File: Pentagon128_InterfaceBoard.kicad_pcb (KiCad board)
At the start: 2 copper layers, 150 x 119 mm, 42 parts, among them J1 DIN41612_02x32_AB, J10 Tape Out, J11 Tape In, J12 Mini-DIN-6, J14 Barrel_Jack_Switch, J2 Conn_02x03_Odd_Even ATmega Pr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, J3 Conn_02x08_Odd_Even Ext Keyb, J4 Conn_02x05_Odd_Even Kempston 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, J5 DE9_Plug Kempston Out SMD, J6 DE15_Plug_HighDensity VGA CRT, J7 Conn_01x04 FDD Power, J8 Conn_01x04 Audio In, J9 AudioJack3, Q1 Q_NPN_BCE, Q2 Q_NPN_BCE, Q3 Q_NPN_BCE, Q4 Q_NPN_BCE, U1 MT8816 PLCC44, U2 ATmega168PA-A

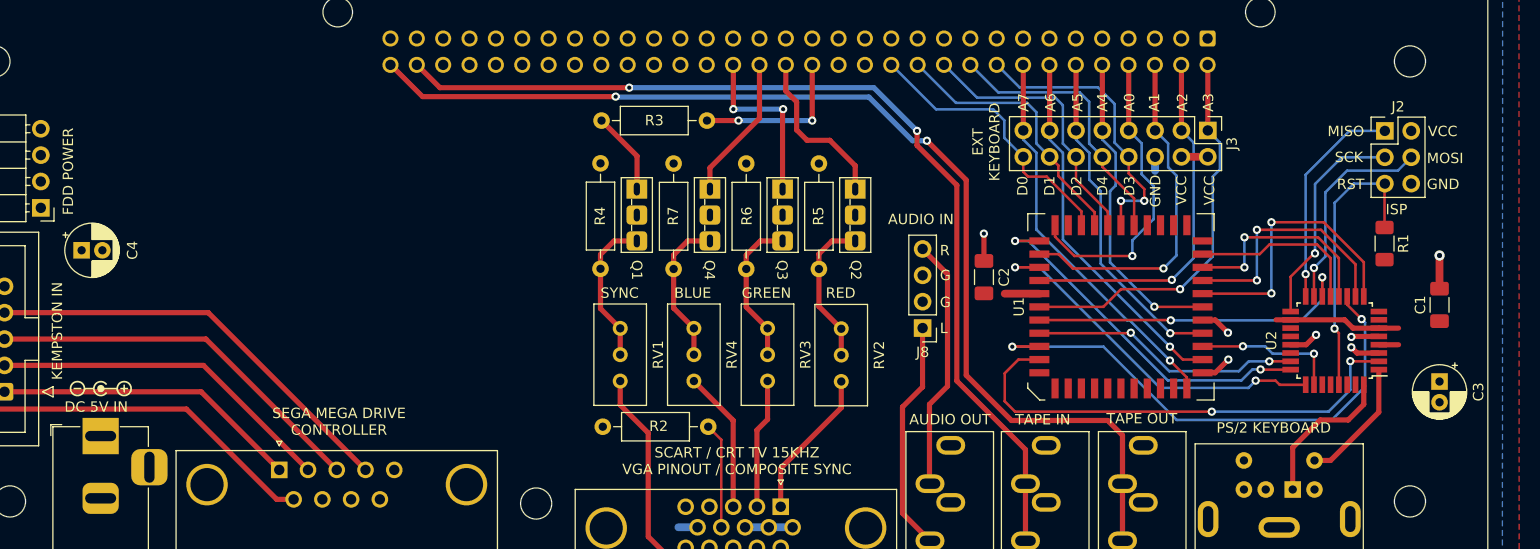
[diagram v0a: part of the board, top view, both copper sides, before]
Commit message: Intermediate variant based on review feedback. Added SN74LS07 oped drain buffers for switch matrix data lines output (questionable). Changes based on "AVR Microcontroller Hardware Design Considerations": - Blocking capacitor for ATmega moved close to power input pins, removed side VCC / GND connections. Not implemented: separate blocking caps for AVCC and all power pins pairs. - Added optional capacitor on ATmega RESET line connected to GND. Removed useless blocking capacitor for MT8816. Removed (possibly) useless electrolytic capacitors from PCB near ATmega and FDC Power connector.
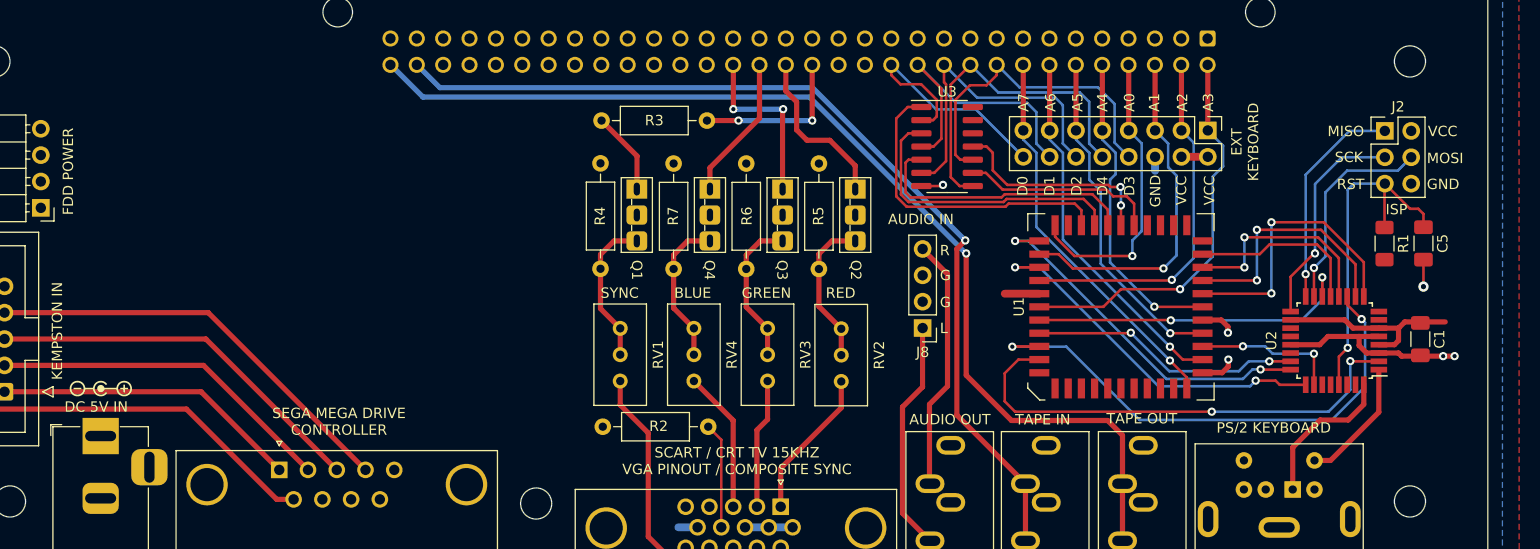
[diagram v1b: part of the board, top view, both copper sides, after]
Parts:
- removed C2: 0.1u, Capacitor_SMD:C_1206_3216Metric_Pad1.33x1.80mm_HandSolder
- removed C3, C4: 10u, Capacitor_THT:CP_Radial_D5.0mm_P2.00mm
- added C5: 0.1u, Capacitor_SMD:C_1206_3216Metric_Pad1.33x1.80mm_HandSolder, F.Cu at (198.4, 83.3)
- added U3: SN74LS07, Package_SO:SOIC-14_3.9x8.7mm_P1.27mm, F.Cu at (152.5, 74.0)
- moved C1 3.78 mm to (198.1, 92.6), turned to -90 degrees
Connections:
- U1 pad 33: /X4 -> Net-(U1-X4)
- U1 pad 34: /X3 -> Net-(U1-X3)
- U1 pad 35: /X2 -> Net-(U1-X2)
- U1 pad 36: /X1 -> Net-(U1-X1)
- U1 pad 37: /X0 -> Net-(U1-X0)
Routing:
- net Net-(U1-X0): track 0.00 -> 30.5 mm
- net Net-(U1-X1): track 0.00 -> 28.4 mm
- net Net-(U1-X2): track 0.00 -> 26.4 mm
- net Net-(U1-X3): track 0.00 -> 20.5 mm, vias 0 -> 2
- net Net-(U1-X4): track 0.00 -> 18.9 mm
- net GND: track 28.0 -> 38.6 mm, vias 7 -> 6
- net /X4: track 26.6 -> 32.8 mm
- net /RST: track 27.5 -> 33.4 mm
- net VCC: track 19.9 -> 24.6 mm
- net /X2: track 26.4 -> 30.7 mm
- net /TAPE_OUT: track 106.5 -> 102.3 mm, vias 2 -> 1
- net /X3: track 28.0 -> 31.7 mm, vias 2 -> 0
- net /TAPE_IN: track 94.6 -> 91.8 mm, vias 2 -> 1
- net /X1: track 26.5 -> 28.4 mm
- net /X0: track 27.3 -> 25.9 mm
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
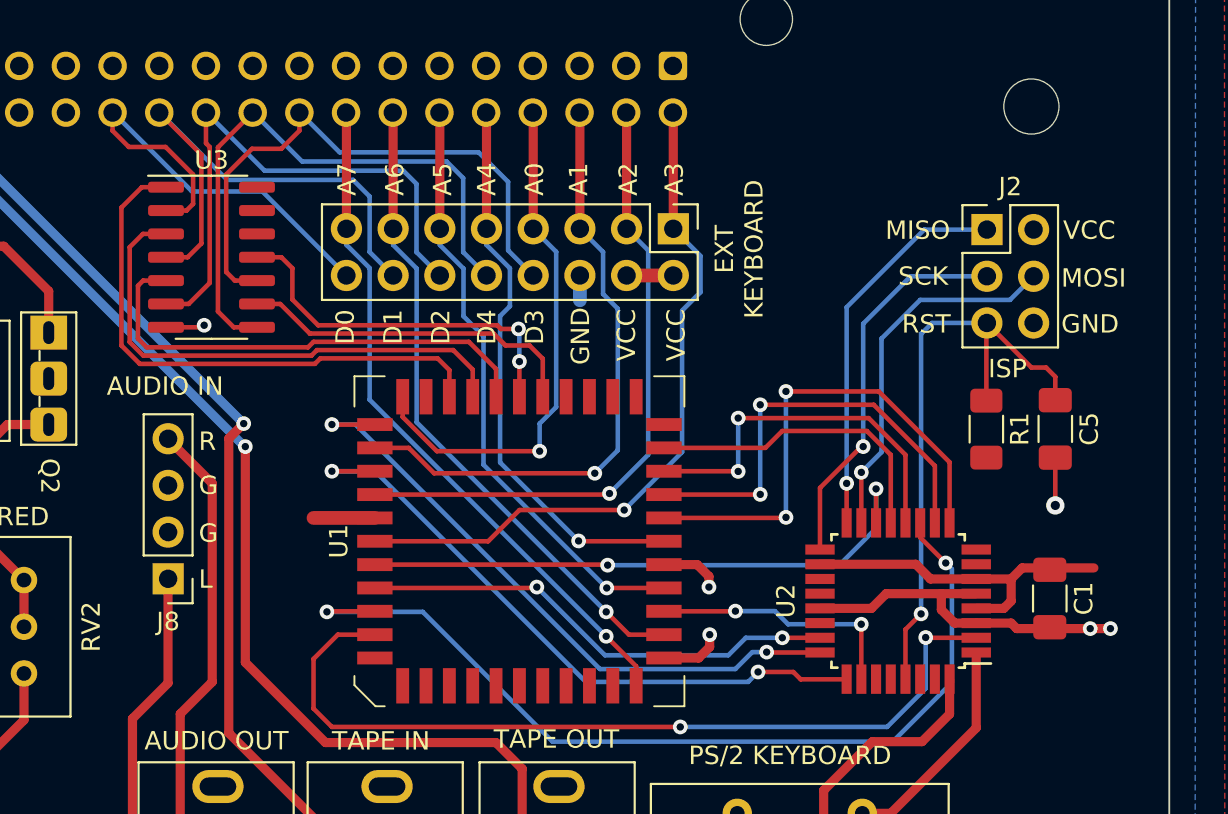
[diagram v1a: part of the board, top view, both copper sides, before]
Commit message: Remove SN74LS07 data bus buffer from schematic and PCB, considering MT8816 switches as switches connecting logical "0" from address bus line to keyboard data bus pulled to "1" (VCC) via pull-up resistors. There is no direct connections of address bus lines to VCC ("1") because of diodes.
Re-enumerate capacitors.
Remove electrolytic capacitors from board.
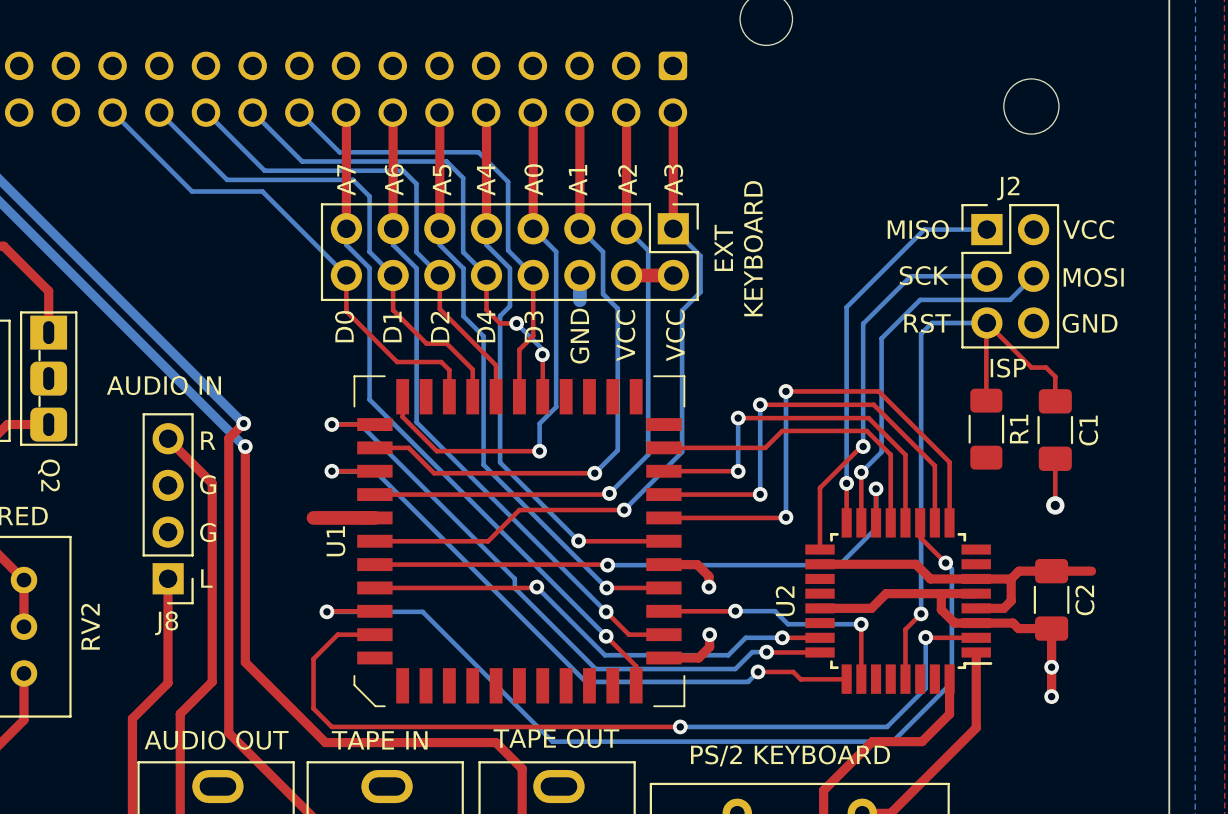
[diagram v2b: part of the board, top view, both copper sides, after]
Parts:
- removed C5: 0.1u, Capacitor_SMD:C_1206_3216Metric_Pad1.33x1.80mm_HandSolder
- removed U3: SN74LS07, Package_SO:SOIC-14_3.9x8.7mm_P1.27mm
- added C2: 0.1u, Capacitor_SMD:C_1206_3216Metric_Pad1.33x1.80mm_HandSolder, F.Cu at (198.2, 92.6)
- moved C1 9.17 mm to (198.4, 83.4)
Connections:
- C1 pad 1: VCC -> /RST
- U1 pad 33: Net-(U1-X4) -> /X4
- U1 pad 34: Net-(U1-X3) -> /X3
- U1 pad 35: Net-(U1-X2) -> /X2
- U1 pad 36: Net-(U1-X1) -> /X1
- U1 pad 37: Net-(U1-X0) -> /X0
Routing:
- net Net-(U1-X0): track 30.5 -> 0.00 mm
- net Net-(U1-X1): track 28.4 -> 0.00 mm
- net Net-(U1-X2): track 26.4 -> 0.00 mm
- net Net-(U1-X3): track 20.5 -> 0.00 mm, vias 2 -> 0
- net Net-(U1-X4): track 18.9 -> 0.00 mm
- net /X3: track 31.7 -> 25.5 mm
- net /X4: track 32.8 -> 27.1 mm, vias 0 -> 2
- net /X2: track 30.7 -> 26.4 mm
- net GND: track 38.6 -> 37.0 mm, vias 6 -> 5
- net /X1: track 28.4 -> 27.2 mm
- net /X0: track 25.9 -> 26.7 mm

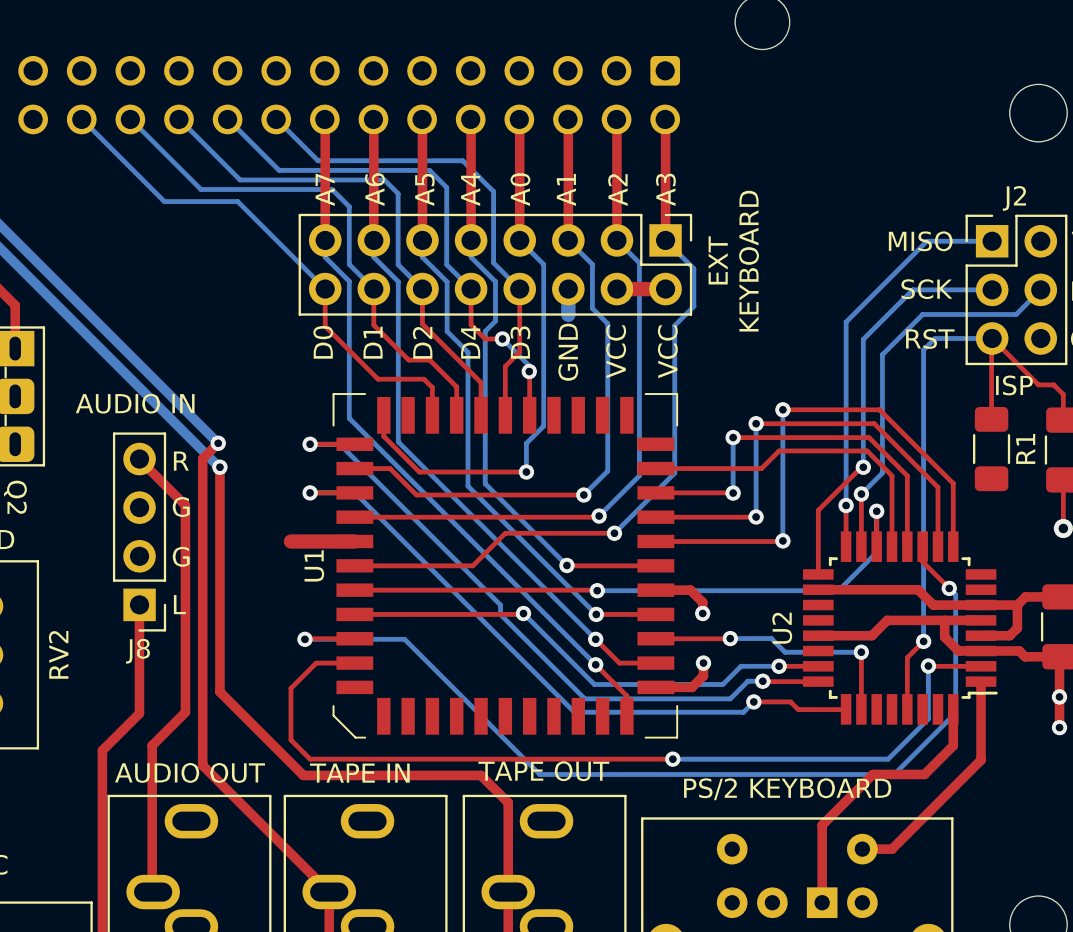
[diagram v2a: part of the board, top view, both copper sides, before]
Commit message: Replace MT8816 pin solder footprint with PLCC-44_THT-Socket.
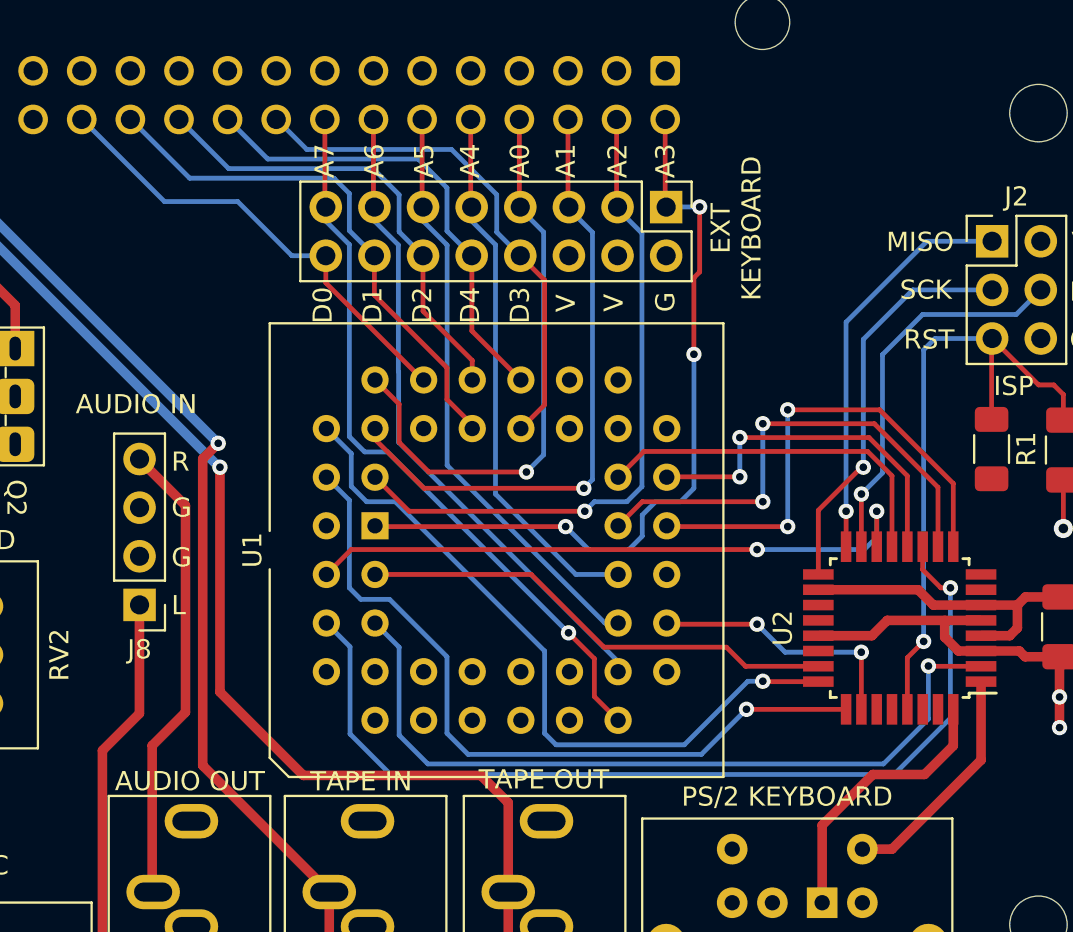
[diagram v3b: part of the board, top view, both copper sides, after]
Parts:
- U1: footprint Package_LCC:PLCC-44 -> Package_LCC:PLCC-44_THT-Socket
- moved U1 7.12 mm to (162.4, 87.4)
- moved J3 1.74 mm to (177.7, 70.7)
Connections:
- J3 pad 2: VCC -> GND
- J3 pad 6: GND -> VCC
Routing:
- net GND: track 37.0 -> 29.0 mm, vias 5 -> 3
- net VCC: track 24.4 -> 18.6 mm
- net /AX0: track 46.7 -> 41.1 mm, vias 2 -> 1
- net /DATA: track 35.5 -> 39.2 mm, vias 2 -> 1
- net /X4: track 27.1 -> 24.4 mm, vias 2 -> 0
- net /X0: track 26.7 -> 24.3 mm
- net /CS: track 35.1 -> 37.4 mm, vias 2 -> 1
- net /AY1: track 17.0 -> 19.1 mm
- net /Y4: track 30.5 -> 28.3 mm, vias 1 -> 0
- net /X2: track 26.4 -> 24.4 mm
- net /Y3: track 38.2 -> 40.1 mm, vias 1 -> 3
- net /Y0: track 28.6 -> 30.4 mm
- net /Y5: track 32.8 -> 31.1 mm, vias 1 -> 0
- net /AX2: track 24.1 -> 25.8 mm
- net /X3: track 25.5 -> 26.9 mm
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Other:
- board text added: "V"
